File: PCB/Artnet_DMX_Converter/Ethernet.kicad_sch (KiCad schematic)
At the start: 98 parts, among them J3 RJ45, T1 FA2805, U4 W5500, U5 VO618A-3X019T, U6 SI3402-B-GMR, U7 TLV431, Y2 ABM8-25.000MHZ-10-D1G-T

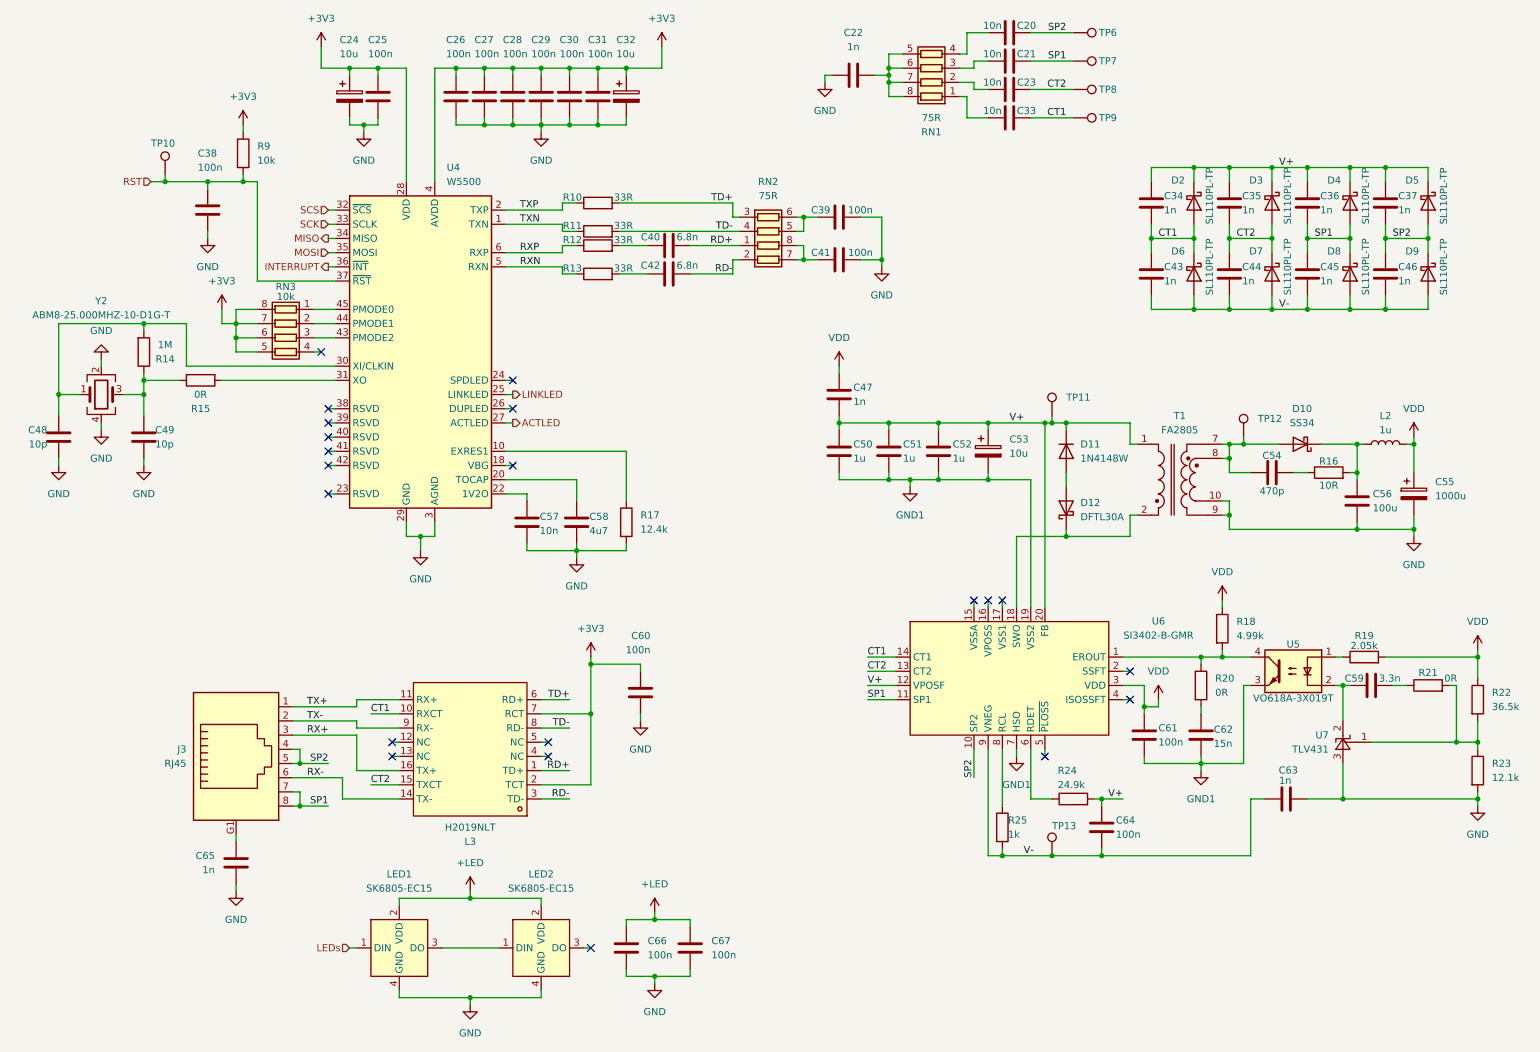
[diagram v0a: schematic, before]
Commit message: Testpoints and GND1 Fill
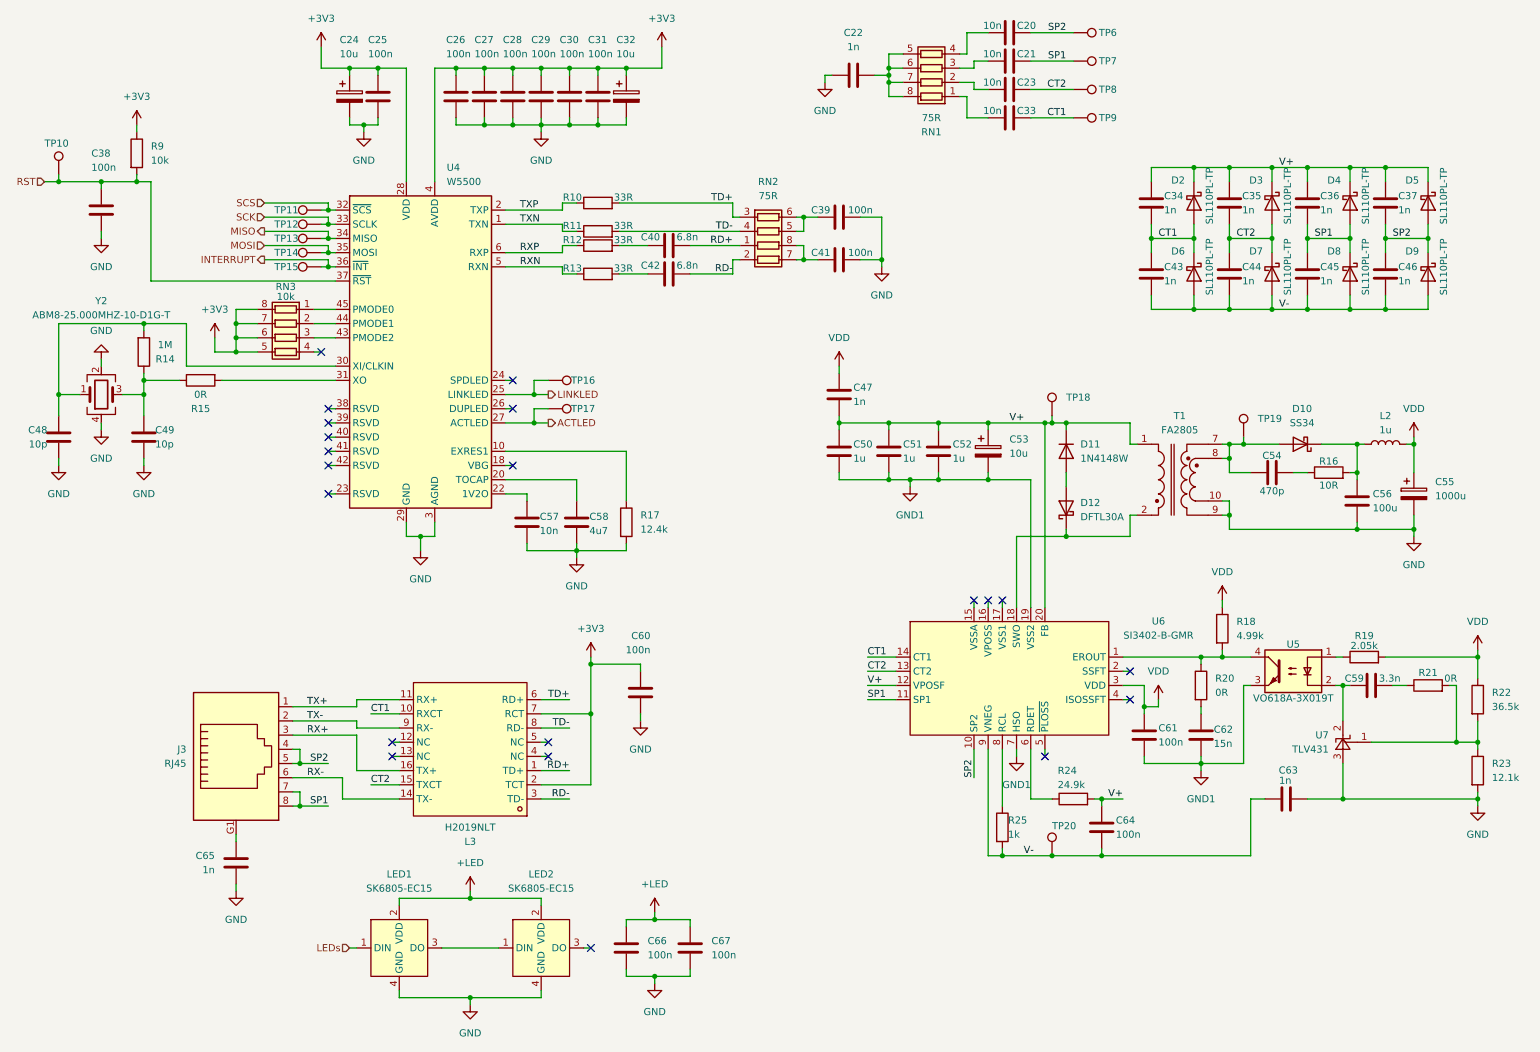
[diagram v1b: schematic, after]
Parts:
- added TP11, TP12, TP13, TP14, TP15, TP16, TP17: TestPoint, TestPoint:TestPoint_Pad_D1.5mm, symbol Connector:TestPoint
- renumbered TP11 to TP18, TP12 to TP19, TP13 to TP20
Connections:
- net ACTLED: now also TP17.1
- net INTERRUPT: now also TP15.1
- net LINKLED: now also TP16.1
- net MISO: now also TP13.1
- net MOSI: now also TP14.1
- net SCK: now also TP12.1
- net SCS: now also TP11.1
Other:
- moved on the sheet: C38, R9, TP10
